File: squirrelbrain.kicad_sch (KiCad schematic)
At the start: 27 parts, among them J1 BM02B-SRSS-TB_LF__SN_, J2 Conn_01x03, J3 BM02B-SRSS-TB_LF__SN_, J4 BATT, J5 BLDC_PWR, J6 GPIO1, U1 RPM5.0-6.0, U2 TPS1HB08BQPWPRQ1, U3 TPS22992SRXNR, U4 SEEEDUINO-XIAO-ESP32S3, U5 THVD1420DRLR, U6 SN74LVC2G125DCUR, U7 THVD1420DRLR

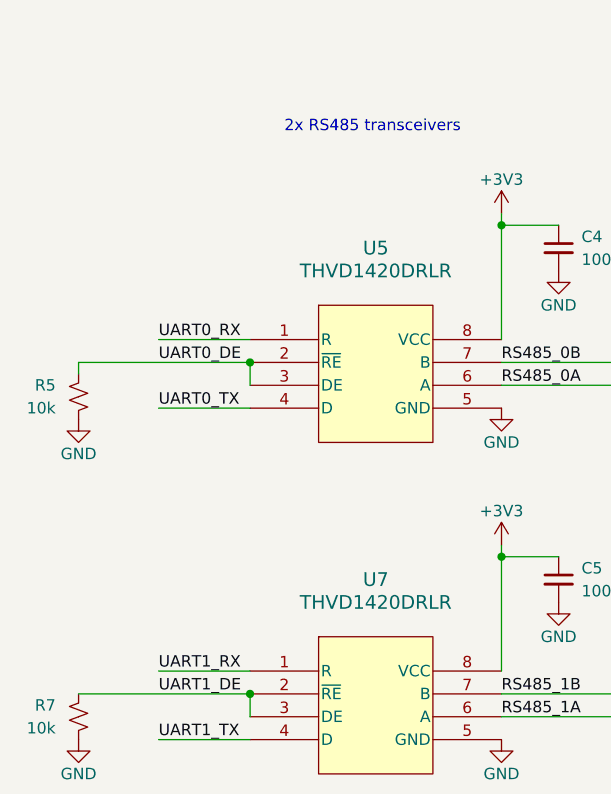
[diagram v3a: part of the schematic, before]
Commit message: rect test pads for 3v3
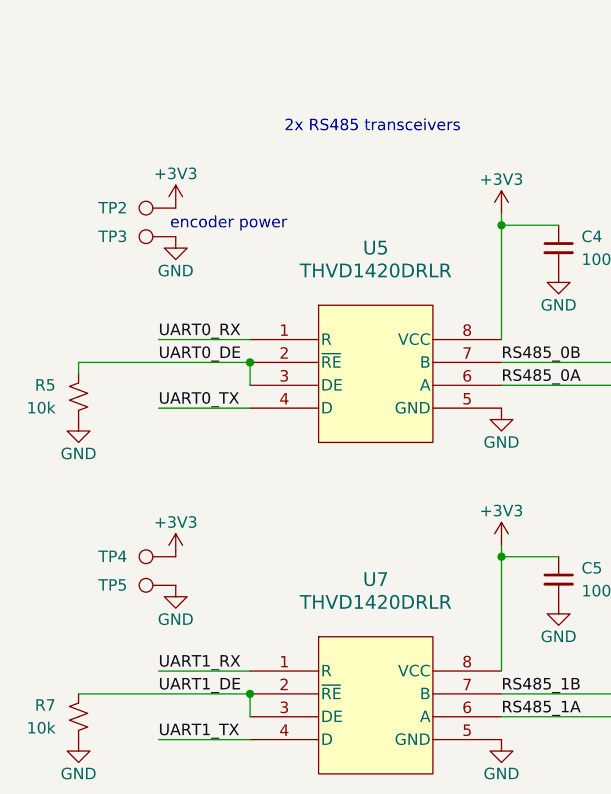
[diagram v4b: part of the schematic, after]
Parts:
- added TP2, TP3, TP4, TP5: TestPoint, squirrelbrain:TestPoint_Pad_Rect, symbol Connector:TestPoint
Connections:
- net +3V3: now also TP2.1, TP4.1
- net GND: now also TP3.1, TP5.1
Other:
- note added: "encoder power"
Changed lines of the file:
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@@
+    (effects (font (size 1.27 1.27)) (justify left bottom))
+  )
+  (text "encoder power" (at 35.56 123.825 0)
     (effects (font (size 1.27 1.27)) (justify left bottom))
   )
@@
   (label "UART0_TX" (at 34.29 143.51 0) (fields_autoplaced)
     (effects (font (size 1.27 1.27)) (justify left bottom))
+  )
+  (symbol (lib_id "Connector:TestPoint") (at 36.195 121.285 90) (unit 1)
+    (in_bom no) (on_board yes) (dnp no)
+    (property "Reference" "TP2" (at 29.21 121.285 90)
+      (effects (font (size 1.27 1.27)))
+    )
+    (property "Value" "TestPoint" (at 26.67 122.555 90)
+      (effects (font (size 1.27 1.27)) hide)
+    )
+    (property "Footprint" "squirrelbrain:TestPoint_Pad_Rect" (at 36.195 116.205 0)
+      (effects (font (size 1.27 1.27)) hide)
+    )
+    (property "Datasheet" "~" (at 36.195 116.205 0)
+      (effects (font (size 1.27 1.27)) hide)
+    )
+    (pin "1")
+    (instances
+      (project "squirrelbrain"
+        (path "/c53f469e-143f-45d2-986d-b1b5b618ea8f"
+          (reference "TP2") (unit 1)
+        )
+      )
+    )
   )
   (symbol (lib_id "power:GND") (at 72.39 143.51 0) (unit 1)
@@
     )
   )
+  (symbol (lib_id "power:+3V3") (at 36.195 160.02 0) (unit 1)
+    (in_bom yes) (on_board yes) (dnp no)
+    (property "Reference" "#PWR041" (at 36.195 163.83 0)
+      (effects (font (size 1.27 1.27)) hide)
+    )
+    (property "Value" "+3V3" (at 36.195 156.21 0)
+      (effects (font (size 1.27 1.27)))
+    )
+    (property "Footprint" "" (at 36.195 160.02 0)
+      (effects (font (size 1.27 1.27)) hide)
+    )
+    (property "Datasheet" "" (at 36.195 160.02 0)
+      (effects (font (size 1.27 1.27)) hide)
+    )
+    (pin "1")
+    (instances
+      (project "squirrelbrain"
+        (path "/c53f469e-143f-45d2-986d-b1b5b618ea8f"
+          (reference "#PWR041") (unit 1)
+        )
+      )
+    )
+  )
   (symbol (lib_id "power:+3V3") (at 72.39 158.75 0) (unit 1)
     (in_bom yes) (on_board yes) (dnp no)
@@
         (path "/c53f469e-143f-45d2-986d-b1b5b618ea8f"
           (reference "#PWR031") (unit 1)
+        )
+      )
+    )
+  )
+  (symbol (lib_id "power:GND") (at 36.195 163.195 0) (unit 1)
+    (in_bom yes) (on_board yes) (dnp no)
+    (property "Reference" "#PWR042" (at 36.195 169.545 0)
+      (effects (font (size 1.27 1.27)) hide)
+    )
+    (property "Value" "GND" (at 36.195 167.005 0)
+      (effects (font (size 1.27 1.27)))
+    )
+    (property "Footprint" "" (at 36.195 163.195 0)
+      (effects (font (size 1.27 1.27)) hide)
+    )
+    (property "Datasheet" "" (at 36.195 163.195 0)
+      (effects (font (size 1.27 1.27)) hide)
+    )
+    (pin "1")
+    (instances
+      (project "squirrelbrain"
+        (path "/c53f469e-143f-45d2-986d-b1b5b618ea8f"
+          (reference "#PWR042") (unit 1)
         )
       )
@@
         (path "/c53f469e-143f-45d2-986d-b1b5b618ea8f"
           (reference "#PWR09") (unit 1)
+        )
+      )
+    )
+  )
+  (symbol (lib_id "Connector:TestPoint") (at 36.195 163.195 90) (unit 1)
+    (in_bom no) (on_board yes) (dnp no)
+    (property "Reference" "TP5" (at 29.21 163.195 90)
+      (effects (font (size 1.27 1.27)))
+    )
+    (property "Value" "TestPoint" (at 26.67 164.465 90)
+      (effects (font (size 1.27 1.27)) hide)
+    )
+    (property "Footprint" "squirrelbrain:TestPoint_Pad_Rect" (at 36.195 158.115 0)
+      (effects (font (size 1.27 1.27)) hide)
+    )
+    (property "Datasheet" "~" (at 36.195 158.115 0)
+      (effects (font (size 1.27 1.27)) hide)
+    )
+    (pin "1")
+    (instances
+      (project "squirrelbrain"
+        (path "/c53f469e-143f-45d2-986d-b1b5b618ea8f"
+          (reference "TP5") (unit 1)
         )
       )
@@
     )
   )
+  (symbol (lib_id "power:+3V3") (at 36.195 121.285 0) (unit 1)
+    (in_bom yes) (on_board yes) (dnp no)
+    (property "Reference" "#PWR039" (at 36.195 125.095 0)
+      (effects (font (size 1.27 1.27)) hide)
+    )
+    (property "Value" "+3V3" (at 36.195 117.475 0)
+      (effects (font (size 1.27 1.27)))
+    )
+    (property "Footprint" "" (at 36.195 121.285 0)
+      (effects (font (size 1.27 1.27)) hide)
+    )
+    (property "Datasheet" "" (at 36.195 121.285 0)
+      (effects (font (size 1.27 1.27)) hide)
+    )
+    (pin "1")
+    (instances
+      (project "squirrelbrain"
+        (path "/c53f469e-143f-45d2-986d-b1b5b618ea8f"
+          (reference "#PWR039") (unit 1)
+        )
+      )
+    )
+  )
   (symbol (lib_id "Connector_Generic:Conn_01x02") (at 30.48 46.99 180) (unit 1)
     (in_bom yes) (on_board yes) (dnp no) (fields_autoplaced)
@@
         (path "/c53f469e-143f-45d2-986d-b1b5b618ea8f"
           (reference "J4") (unit 1)
+        )
+      )
+    )
+  )
+  (symbol (lib_id "Connector:TestPoint") (at 36.195 160.02 90) (unit 1)
+    (in_bom no) (on_board yes) (dnp no)
+    (property "Reference" "TP4" (at 29.21 160.02 90)
+      (effects (font (size 1.27 1.27)))
+    )
+    (property "Value" "TestPoint" (at 26.67 161.29 90)
+      (effects (font (size 1.27 1.27)) hide)
+    )
+    (property "Footprint" "squirrelbrain:TestPoint_Pad_Rect" (at 36.195 154.94 0)
+      (effects (font (size 1.27 1.27)) hide)
+    )
+    (property "Datasheet" "~" (at 36.195 154.94 0)
+      (effects (font (size 1.27 1.27)) hide)
+    )
+    (pin "1")
+    (instances
+      (project "squirrelbrain"
+        (path "/c53f469e-143f-45d2-986d-b1b5b618ea8f"
+          (reference "TP4") (unit 1)
         )
       )
@@
     )
   )
+  (symbol (lib_id "power:GND") (at 36.195 124.46 0) (unit 1)
+    (in_bom yes) (on_board yes) (dnp no)
+    (property "Reference" "#PWR040" (at 36.195 130.81 0)
+      (effects (font (size 1.27 1.27)) hide)
+    )
+    (property "Value" "GND" (at 36.195 128.27 0)
+      (effects (font (size 1.27 1.27)))
+    )
+    (property "Footprint" "" (at 36.195 124.46 0)
+      (effects (font (size 1.27 1.27)) hide)
+    )
+    (property "Datasheet" "" (at 36.195 124.46 0)
+      (effects (font (size 1.27 1.27)) hide)
+    )
+    (pin "1")
+    (instances
+      (project "squirrelbrain"
+        (path "/c53f469e-143f-45d2-986d-b1b5b618ea8f"
+          (reference "#PWR040") (unit 1)
+        )
+      )
+    )
+  )
   (symbol (lib_id "power:GND") (at 107.95 172.72 0) (unit 1)
     (in_bom yes) (on_board yes) (dnp no)
@@
         )
       )
+    )
+  )
+  (symbol (lib_id "Connector:TestPoint") (at 36.195 124.46 90) (unit 1)
+    (in_bom no) (on_board yes) (dnp no)
+    (property "Reference" "TP3" (at 29.21 124.46 90)
+      (effects (font (size 1.27 1.27)))
+    )
+    (property "Value" "TestPoint" (at 26.67 125.73 90)
+      (effects (font (size 1.27 1.27)) hide)
+    )
+    (property "Footprint" "squirrelbrain:TestPoint_Pad_Rect" (at 36.195 119.38 0)
+      (effects (font (size 1.27 1.27)) hide)
+    )
+    (property "Datasheet" "~" (at 36.195 119.38 0)
+      (effects (font (size 1.27 1.27)) hide)
+    )
+    (pin "1")
+    (instances
+      (project "squirrelbrain"
+        (path "/c53f469e-143f-45d2-986d-b1b5b618ea8f"
+          (reference "TP3") (unit 1)
+        )
+      )

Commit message: generate gerbers
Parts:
- removed R4: 10k, Resistor_SMD:R_0402_1005Metric, symbol Device:R_Small_US
- added R9: 1k, Resistor_SMD:R_0402_1005Metric, symbol Device:R_Small_US
- added TP1, TP6: TestPoint, squirrelbrain:TestPoint_Pad_Rect, symbol Connector:TestPoint
- R1: value 1k -> 390R; MP RC0402FR-071KL -> RC0402FR-07390RL; Vendor # 311-1.00KLRCT-ND -> 311-390LRCT-ND
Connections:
- net GND: now also TP6.1
- net MOTOR_ON: now also R9.1, TP1.1; no longer U4.1 (PA02_A0_D0)
- new net: R9.2, U4.1 (PA02_A0_D0)
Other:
- note added: "short these to power off motors"
- moved on the sheet: J6

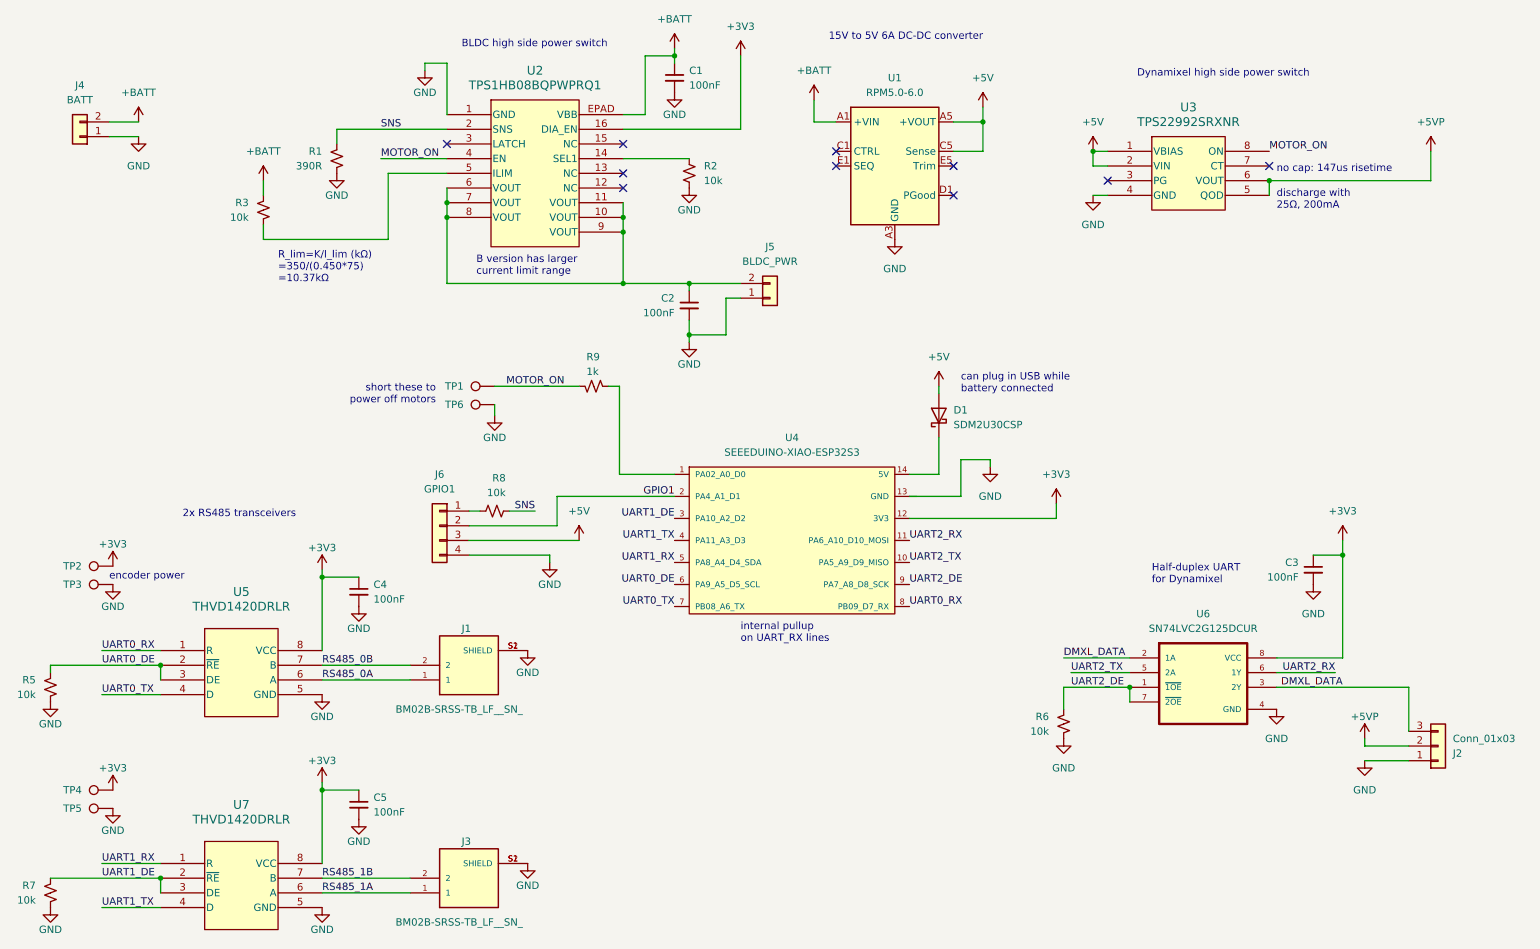
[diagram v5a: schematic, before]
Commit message: add schematic labels just for reference
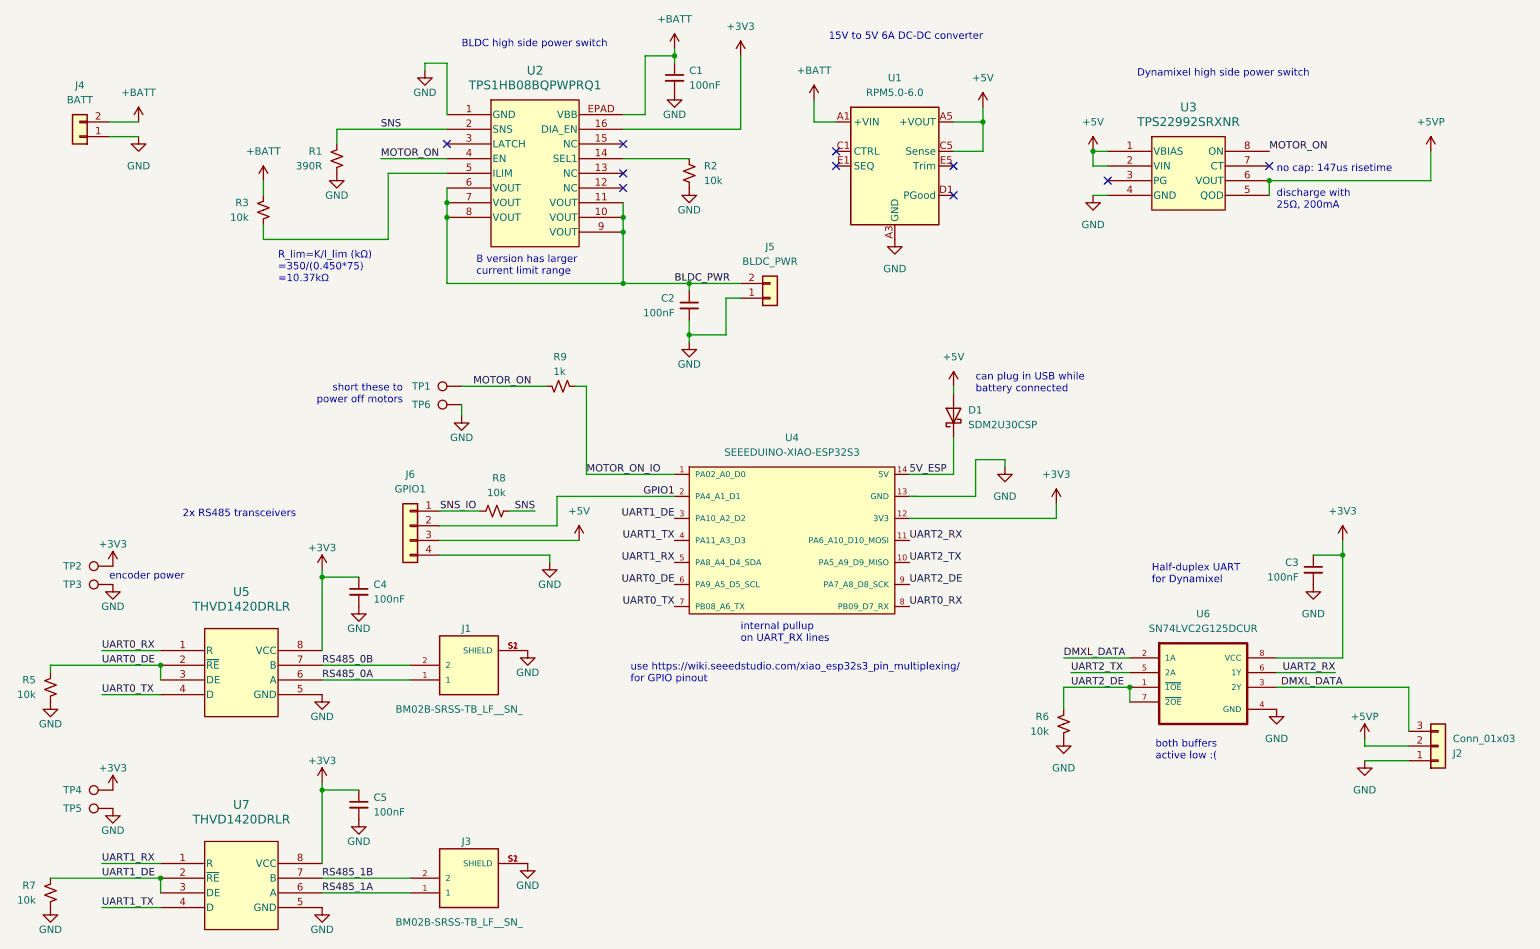
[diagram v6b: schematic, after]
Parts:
- C1, C2, C3, C4, C5: Vendor Digikey -> LCSC; Vendor # (none) -> C14663
- D1: Vendor (none) -> LCSC; Vendor # (none) -> C3001723
- J1, J3: Vendor (none) -> LCSC; Vendor # (none) -> C160388
- J2: Vendor Digikey -> LCSC; Vendor # 455-B3B-EH-A-ND -> C160259
- R1: Vendor Digikey -> LCSC; Vendor # 311-390LRCT-ND -> C137997
- R2, R3, R5, R6, R7, R8, R9: Vendor Digikey -> Inventory
- U4: Vendor (none) -> Seeedstudio
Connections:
- net SNS_IO: now reaches J6.1 (Pin_1), R8.2
- net 5V_ESP: now reaches D1.1 (K), U4.14 (5V)
- net MOTOR_ON_IO: now reaches R9.2, U4.1 (PA02_A0_D0)
- net BLDC_PWR: now reaches C2.1, J5.2 (Pin_2), U2.10 (VOUT), U2.11 (VOUT), U2.6 (VOUT), U2.7 (VOUT), U2.8 (VOUT), U2.9 (VOUT)
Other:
- note added: "both buffers active low :("
- note added: "use https://wiki.seeedstudio.com/xiao_esp32s3_pin_multiplexing/ for GPIO pinout"
- moved on the sheet: D1, J6, R9, TP1, TP6
